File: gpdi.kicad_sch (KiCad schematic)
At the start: 21 parts, among them U11 PCA9306D

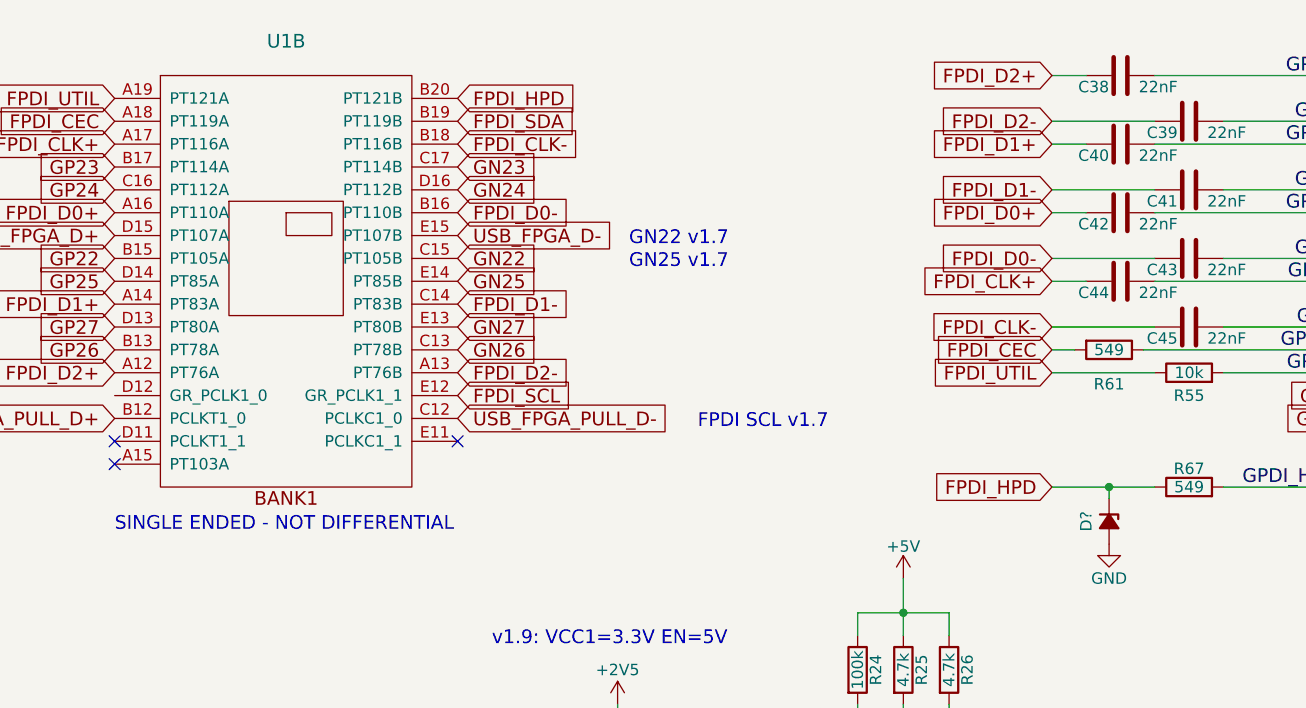
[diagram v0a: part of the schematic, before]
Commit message: Adding USB-C
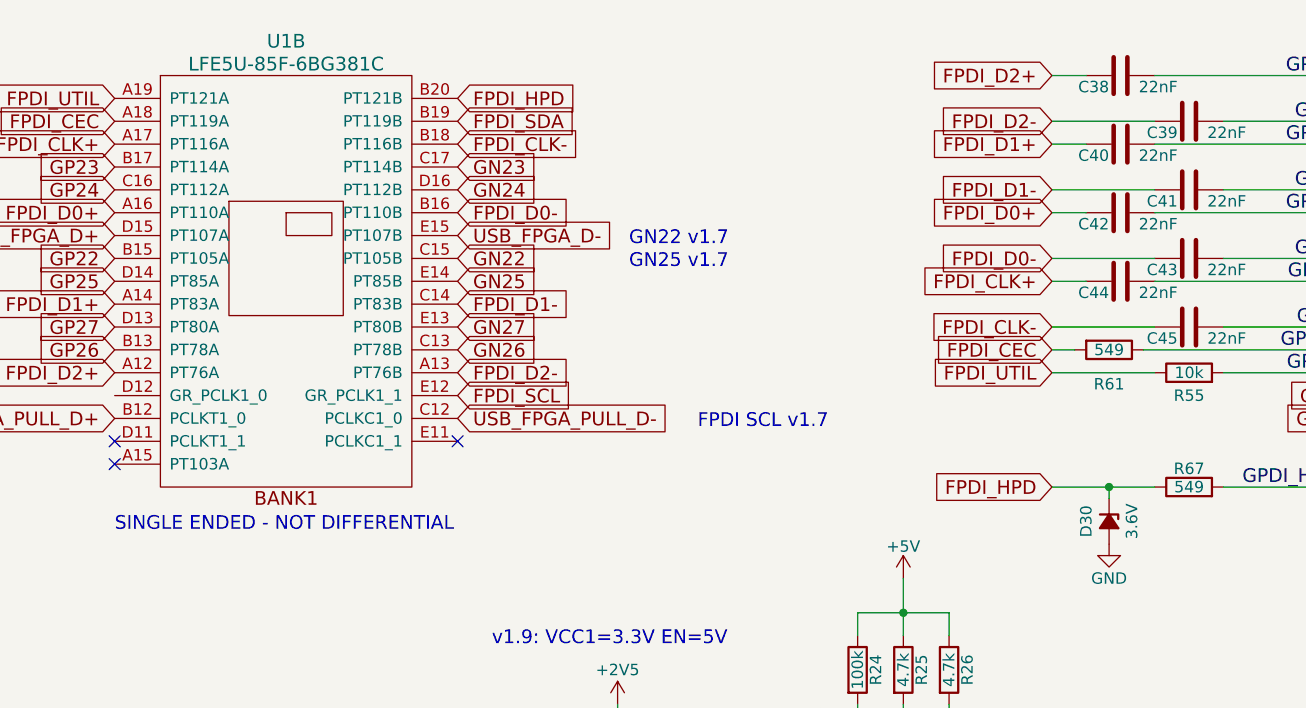
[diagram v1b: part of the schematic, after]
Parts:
- D30: renamed from D?; value (none) -> 3.6V; footprint (none) -> Diode_SMD:D_SOD-323_HandSoldering
- U1: value (none) -> LFE5U-85F-6BG381C; footprint (none) -> lfe5bg381:BGA-381_pitch0.8mm_dia0.4mm
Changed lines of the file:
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@@
   (title_block
     (title "ULX3S")
-    (rev "1.0.5")
+    (date "2023-01-19")
+    (rev "3.1.8")
     (company "EMARD")
     (comment 1 "General Purpose Differential Interface")
@@
       (effects (font (size 1.524 1.524)))
     )
-    (property "Value" "" (id 1) (at 91.44 52.07 0)
+    (property "Value" "LFE5U-85F-6BG381C" (id 1) (at 91.44 52.07 0)
       (effects (font (size 1.524 1.524)))
     )
-    (property "Footprint" "" (id 2) (at 64.77 49.53 0)
+    (property "Footprint" "lfe5bg381:BGA-381_pitch0.8mm_dia0.4mm" (id 2) (at 64.77 49.53 0)
       (effects (font (size 1.524 1.524)) hide)
     )
@@
   (symbol (lib_id "ulx3s-rescue:D_Zener_Small_ALT-Device") (at 182.88 102.87 270) (unit 1)
     (in_bom yes) (on_board yes)
-    (property "Reference" "D?" (id 0) (at 180.34 102.87 0))
-    (property "Value" "" (id 1) (at 185.42 102.87 0))
-    (property "Footprint" "" (id 2) (at 182.88 102.87 90)
-      (effects (font (size 1.27 1.27)) hide)
-    )
+    (property "Reference" "D30" (id 0) (at 180.34 102.87 0))
+    (property "Value" "3.6V" (id 1) (at 185.42 102.87 0))
+    (property "Footprint" "Diode_SMD:D_SOD-323_HandSoldering" (id 2) (at 182.88 102.87 90)
+      (effects (font (size 1.27 1.27)) hide)
+    )
